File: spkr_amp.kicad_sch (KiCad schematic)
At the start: 6 parts, among them U2 TPA2006D1DRBR

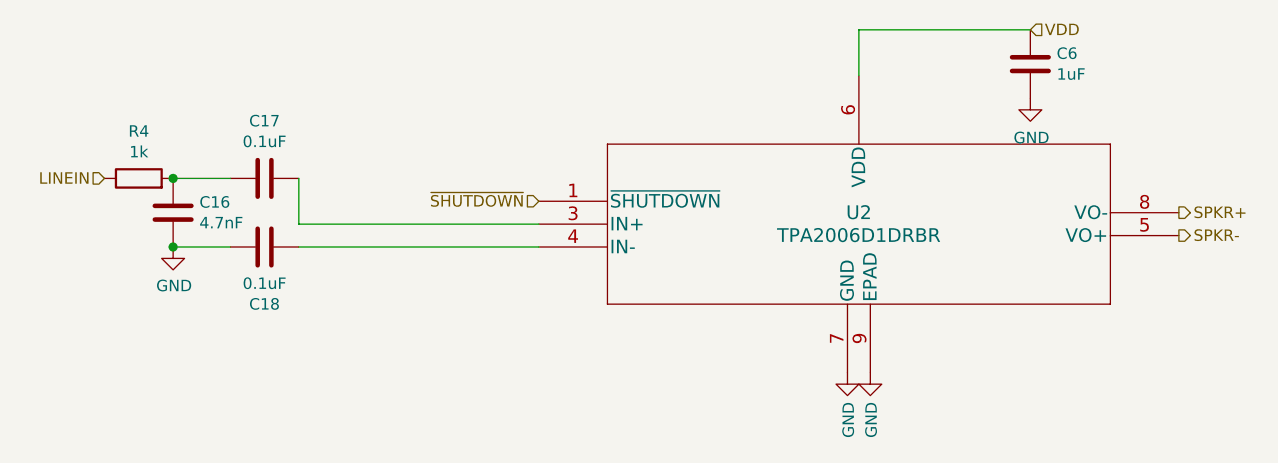
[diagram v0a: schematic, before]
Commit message: Start refactoring board to use Radxa Rock 3 Compute Module instead of Raspberry Pi CM4.
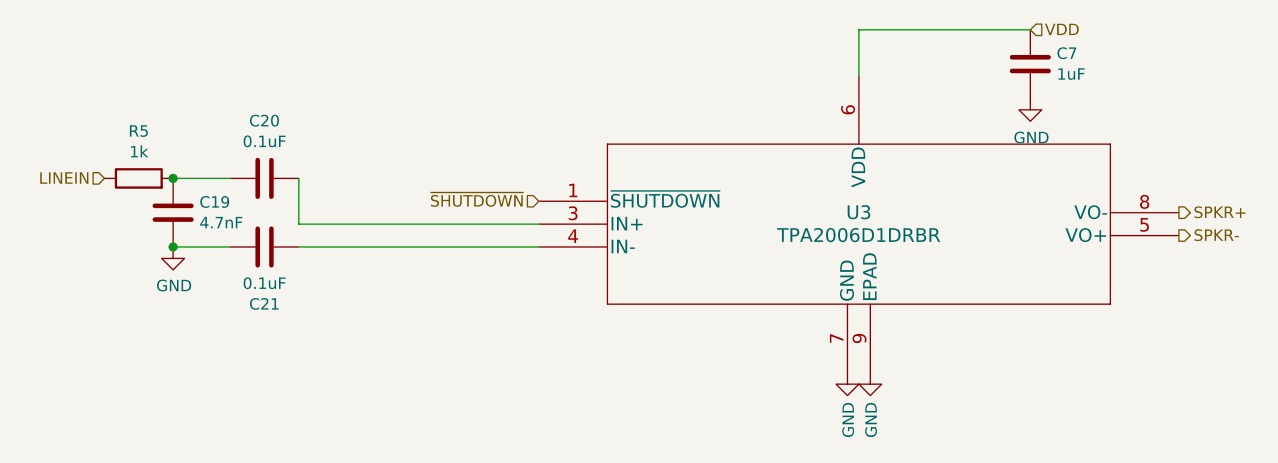
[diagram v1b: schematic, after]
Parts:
- renumbered C16 to C19, C17 to C20, C18 to C21, C6 to C7, R4 to R5, U2 to U3
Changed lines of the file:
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@@
   (symbol (lib_id "Device:R") (at 91.44 78.74 90)
     (in_bom yes) (on_board yes)
-    (property "Reference" "R4" (id 0) (at 91.44 73.5138 90))
+    (property "Reference" "R5" (id 0) (at 91.44 73.5138 90))
     (property "Value" "1k" (id 1) (at 91.44 75.812 90))
     (property "Footprint" "Resistor_SMD:R_0402_1005Metric" (id 2) (at 91.44 80.518 90)
@@
   (symbol (lib_id "Device:C") (at 95.25 82.55 0)
     (in_bom yes) (on_board yes)
-    (property "Reference" "C16" (id 0) (at 98.1711 81.4006 0)
+    (property "Reference" "C19" (id 0) (at 98.1711 81.4006 0)
       (effects (font (size 1.27 1.27)) (justify left))
     )
@@
   (symbol (lib_id "Device:C") (at 105.41 78.74 90)
     (in_bom yes) (on_board yes)
-    (property "Reference" "C17" (id 0) (at 105.41 72.3708 90))
+    (property "Reference" "C20" (id 0) (at 105.41 72.3708 90))
     (property "Value" "0.1uF" (id 1) (at 105.41 74.669 90))
     (property "Footprint" "Capacitor_SMD:C_0402_1005Metric" (id 2) (at 109.22 77.7748 0)
@@
   (symbol (lib_id "Device:C") (at 105.41 86.36 90)
     (in_bom yes) (on_board yes)
-    (property "Reference" "C18" (id 0) (at 105.41 92.7292 90))
+    (property "Reference" "C21" (id 0) (at 105.41 92.7292 90))
     (property "Value" "0.1uF" (id 1) (at 105.41 90.43 90))
     (property "Footprint" "Capacitor_SMD:C_0402_1005Metric" (id 2) (at 109.22 85.3948 0)
@@
   (symbol (lib_id "Device:C") (at 190.5 66.04 0)
     (in_bom yes) (on_board yes)
-    (property "Reference" "C6" (id 0) (at 193.421 64.8716 0)
+    (property "Reference" "C7" (id 0) (at 193.421 64.8716 0)
       (effects (font (size 1.27 1.27)) (justify left))
     )
@@
   (symbol (lib_id "TPA2006D1DRBR:TPA2006D1DRBR") (at 171.45 83.82 0)
     (in_bom yes) (on_board yes)
-    (property "Reference" "U2" (id 0) (at 171.45 82.55 0)
+    (property "Reference" "U3" (id 0) (at 171.45 82.55 0)
       (effects (font (size 1.524 1.524)))
     )

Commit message: WIP: start reworking board to use CM4 instead of 40-pin connector
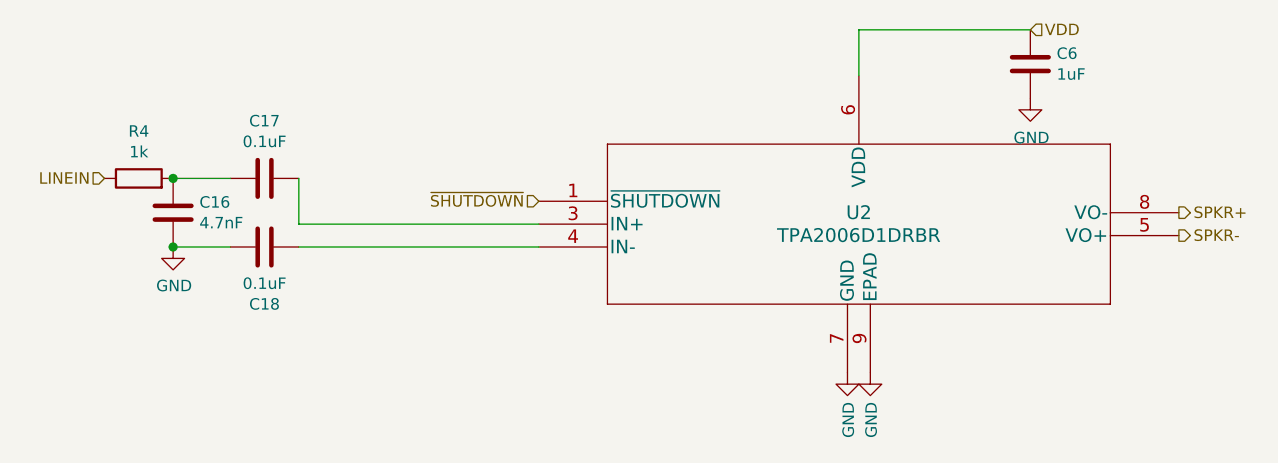
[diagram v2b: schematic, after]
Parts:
- renumbered C19 to C16, C20 to C17, C21 to C18, C7 to C6, R5 to R4, U3 to U2
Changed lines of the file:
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@@
   (symbol (lib_id "Device:R") (at 91.44 78.74 90)
     (in_bom yes) (on_board yes)
-    (property "Reference" "R5" (id 0) (at 91.44 73.5138 90))
+    (property "Reference" "R4" (id 0) (at 91.44 73.5138 90))
     (property "Value" "1k" (id 1) (at 91.44 75.812 90))
     (property "Footprint" "Resistor_SMD:R_0402_1005Metric" (id 2) (at 91.44 80.518 90)
@@
   (symbol (lib_id "Device:C") (at 95.25 82.55 0)
     (in_bom yes) (on_board yes)
-    (property "Reference" "C19" (id 0) (at 98.1711 81.4006 0)
+    (property "Reference" "C16" (id 0) (at 98.1711 81.4006 0)
       (effects (font (size 1.27 1.27)) (justify left))
     )
@@
   (symbol (lib_id "Device:C") (at 105.41 78.74 90)
     (in_bom yes) (on_board yes)
-    (property "Reference" "C20" (id 0) (at 105.41 72.3708 90))
+    (property "Reference" "C17" (id 0) (at 105.41 72.3708 90))
     (property "Value" "0.1uF" (id 1) (at 105.41 74.669 90))
     (property "Footprint" "Capacitor_SMD:C_0402_1005Metric" (id 2) (at 109.22 77.7748 0)
@@
   (symbol (lib_id "Device:C") (at 105.41 86.36 90)
     (in_bom yes) (on_board yes)
-    (property "Reference" "C21" (id 0) (at 105.41 92.7292 90))
+    (property "Reference" "C18" (id 0) (at 105.41 92.7292 90))
     (property "Value" "0.1uF" (id 1) (at 105.41 90.43 90))
     (property "Footprint" "Capacitor_SMD:C_0402_1005Metric" (id 2) (at 109.22 85.3948 0)
@@
   (symbol (lib_id "Device:C") (at 190.5 66.04 0)
     (in_bom yes) (on_board yes)
-    (property "Reference" "C7" (id 0) (at 193.421 64.8716 0)
+    (property "Reference" "C6" (id 0) (at 193.421 64.8716 0)
       (effects (font (size 1.27 1.27)) (justify left))
     )
@@
   (symbol (lib_id "TPA2006D1DRBR:TPA2006D1DRBR") (at 171.45 83.82 0)
     (in_bom yes) (on_board yes)
-    (property "Reference" "U3" (id 0) (at 171.45 82.55 0)
+    (property "Reference" "U2" (id 0) (at 171.45 82.55 0)
       (effects (font (size 1.524 1.524)))
     )

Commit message: WIP: Flip the touchscreen connectors. Fixes #2.
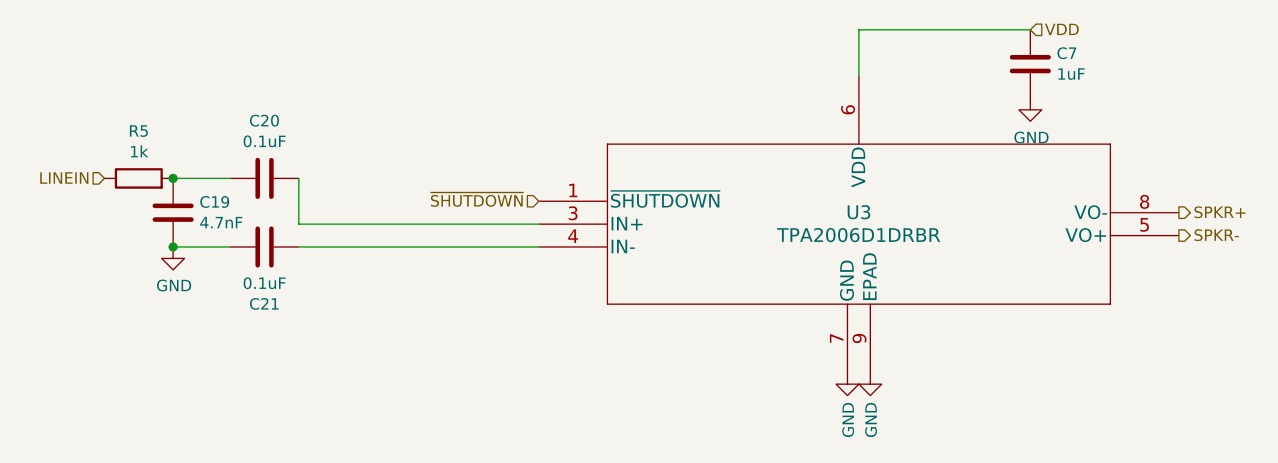
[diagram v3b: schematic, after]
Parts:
- renumbered C16 to C19, C17 to C20, C18 to C21, C6 to C7, R4 to R5, U2 to U3
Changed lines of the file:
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@@
   (symbol (lib_id "power:GND") (at 95.25 86.36 0)
     (in_bom yes) (on_board yes)
-    (property "Reference" "#PWR0112" (id 0) (at 95.25 92.71 0)
+    (property "Reference" "#PWR0105" (id 0) (at 95.25 92.71 0)
       (effects (font (size 1.27 1.27)) hide)
     )
@@
   (symbol (lib_id "power:GND") (at 170.18 100.33 0)
     (in_bom yes) (on_board yes)
-    (property "Reference" "#PWR0116" (id 0) (at 170.18 106.68 0)
+    (property "Reference" "#PWR0107" (id 0) (at 170.18 106.68 0)
       (effects (font (size 1.27 1.27)) hide)
     )
@@
   (symbol (lib_id "power:GND") (at 172.72 100.33 0)
     (in_bom yes) (on_board yes)
-    (property "Reference" "#PWR0117" (id 0) (at 172.72 106.68 0)
+    (property "Reference" "#PWR0108" (id 0) (at 172.72 106.68 0)
       (effects (font (size 1.27 1.27)) hide)
     )
@@
   (symbol (lib_id "power:GND") (at 190.5 69.85 0)
     (in_bom yes) (on_board yes)
-    (property "Reference" "#PWR0118" (id 0) (at 190.5 76.2 0)
+    (property "Reference" "#PWR0110" (id 0) (at 190.5 76.2 0)
       (effects (font (size 1.27 1.27)) hide)
     )
@@
   (symbol (lib_id "Device:R") (at 91.44 78.74 90)
     (in_bom yes) (on_board yes)
-    (property "Reference" "R4" (id 0) (at 91.44 73.5138 90))
+    (property "Reference" "R5" (id 0) (at 91.44 73.5138 90))
     (property "Value" "1k" (id 1) (at 91.44 75.812 90))
     (property "Footprint" "Resistor_SMD:R_0402_1005Metric" (id 2) (at 91.44 80.518 90)
@@
   (symbol (lib_id "Device:C") (at 95.25 82.55 0)
     (in_bom yes) (on_board yes)
-    (property "Reference" "C16" (id 0) (at 98.1711 81.4006 0)
+    (property "Reference" "C19" (id 0) (at 98.1711 81.4006 0)
       (effects (font (size 1.27 1.27)) (justify left))
     )
@@
   (symbol (lib_id "Device:C") (at 105.41 78.74 90)
     (in_bom yes) (on_board yes)
-    (property "Reference" "C17" (id 0) (at 105.41 72.3708 90))
+    (property "Reference" "C20" (id 0) (at 105.41 72.3708 90))
     (property "Value" "0.1uF" (id 1) (at 105.41 74.669 90))
     (property "Footprint" "Capacitor_SMD:C_0402_1005Metric" (id 2) (at 109.22 77.7748 0)
@@
   (symbol (lib_id "Device:C") (at 105.41 86.36 90)
     (in_bom yes) (on_board yes)
-    (property "Reference" "C18" (id 0) (at 105.41 92.7292 90))
+    (property "Reference" "C21" (id 0) (at 105.41 92.7292 90))
     (property "Value" "0.1uF" (id 1) (at 105.41 90.43 90))
     (property "Footprint" "Capacitor_SMD:C_0402_1005Metric" (id 2) (at 109.22 85.3948 0)
@@
   (symbol (lib_id "Device:C") (at 190.5 66.04 0)
     (in_bom yes) (on_board yes)
-    (property "Reference" "C6" (id 0) (at 193.421 64.8716 0)
+    (property "Reference" "C7" (id 0) (at 193.421 64.8716 0)
       (effects (font (size 1.27 1.27)) (justify left))
     )
@@
   (symbol (lib_id "TPA2006D1DRBR:TPA2006D1DRBR") (at 171.45 83.82 0)
     (in_bom yes) (on_board yes)
-    (property "Reference" "U2" (id 0) (at 171.45 82.55 0)
+    (property "Reference" "U3" (id 0) (at 171.45 82.55 0)
       (effects (font (size 1.524 1.524)))
     )

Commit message: Add dock connector, battery pads, and ambient light sensor/compass connector. Switch Pi GPIO header from from THT to SMT so it is easier to place/route. Route differential signals for LVDS converter.
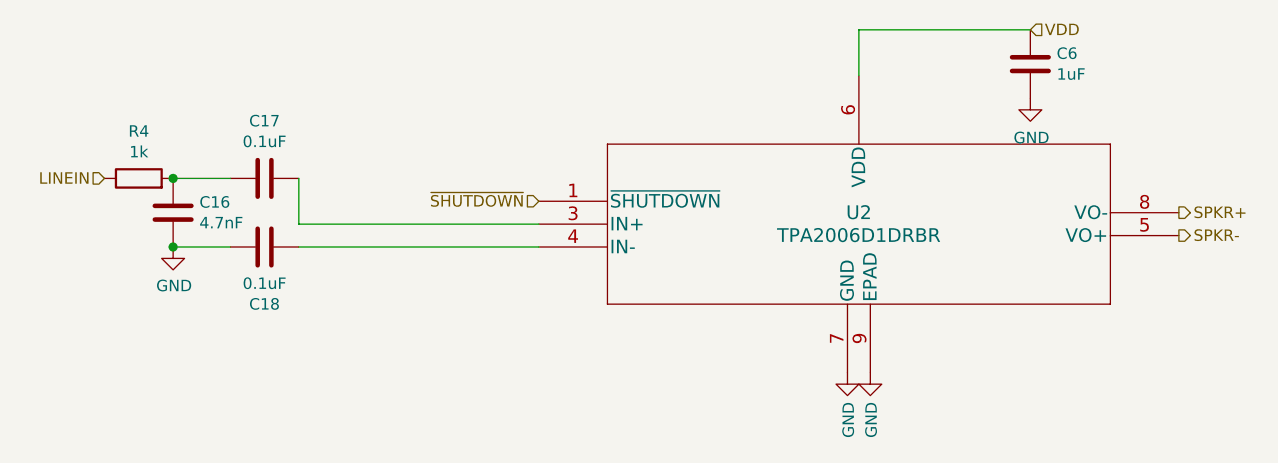
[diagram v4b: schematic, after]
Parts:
- renumbered C19 to C16, C20 to C17, C21 to C18, C7 to C6, R5 to R4, U3 to U2
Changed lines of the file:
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@@
   (symbol (lib_id "power:GND") (at 95.25 86.36 0)
     (in_bom yes) (on_board yes)
-    (property "Reference" "#PWR0105" (id 0) (at 95.25 92.71 0)
+    (property "Reference" "#PWR0112" (id 0) (at 95.25 92.71 0)
       (effects (font (size 1.27 1.27)) hide)
     )
@@
   (symbol (lib_id "power:GND") (at 170.18 100.33 0)
     (in_bom yes) (on_board yes)
-    (property "Reference" "#PWR0107" (id 0) (at 170.18 106.68 0)
+    (property "Reference" "#PWR0116" (id 0) (at 170.18 106.68 0)
       (effects (font (size 1.27 1.27)) hide)
     )
@@
   (symbol (lib_id "power:GND") (at 172.72 100.33 0)
     (in_bom yes) (on_board yes)
-    (property "Reference" "#PWR0108" (id 0) (at 172.72 106.68 0)
+    (property "Reference" "#PWR0117" (id 0) (at 172.72 106.68 0)
       (effects (font (size 1.27 1.27)) hide)
     )
@@
   (symbol (lib_id "power:GND") (at 190.5 69.85 0)
     (in_bom yes) (on_board yes)
-    (property "Reference" "#PWR0110" (id 0) (at 190.5 76.2 0)
+    (property "Reference" "#PWR0118" (id 0) (at 190.5 76.2 0)
       (effects (font (size 1.27 1.27)) hide)
     )
@@
   (symbol (lib_id "Device:R") (at 91.44 78.74 90)
     (in_bom yes) (on_board yes)
-    (property "Reference" "R5" (id 0) (at 91.44 73.5138 90))
+    (property "Reference" "R4" (id 0) (at 91.44 73.5138 90))
     (property "Value" "1k" (id 1) (at 91.44 75.812 90))
     (property "Footprint" "Resistor_SMD:R_0402_1005Metric" (id 2) (at 91.44 80.518 90)
@@
   (symbol (lib_id "Device:C") (at 95.25 82.55 0)
     (in_bom yes) (on_board yes)
-    (property "Reference" "C19" (id 0) (at 98.1711 81.4006 0)
+    (property "Reference" "C16" (id 0) (at 98.1711 81.4006 0)
       (effects (font (size 1.27 1.27)) (justify left))
     )
@@
   (symbol (lib_id "Device:C") (at 105.41 78.74 90)
     (in_bom yes) (on_board yes)
-    (property "Reference" "C20" (id 0) (at 105.41 72.3708 90))
+    (property "Reference" "C17" (id 0) (at 105.41 72.3708 90))
     (property "Value" "0.1uF" (id 1) (at 105.41 74.669 90))
     (property "Footprint" "Capacitor_SMD:C_0402_1005Metric" (id 2) (at 109.22 77.7748 0)
@@
   (symbol (lib_id "Device:C") (at 105.41 86.36 90)
     (in_bom yes) (on_board yes)
-    (property "Reference" "C21" (id 0) (at 105.41 92.7292 90))
+    (property "Reference" "C18" (id 0) (at 105.41 92.7292 90))
     (property "Value" "0.1uF" (id 1) (at 105.41 90.43 90))
     (property "Footprint" "Capacitor_SMD:C_0402_1005Metric" (id 2) (at 109.22 85.3948 0)
@@
   (symbol (lib_id "Device:C") (at 190.5 66.04 0)
     (in_bom yes) (on_board yes)
-    (property "Reference" "C7" (id 0) (at 193.421 64.8716 0)
+    (property "Reference" "C6" (id 0) (at 193.421 64.8716 0)
       (effects (font (size 1.27 1.27)) (justify left))
     )
@@
   (symbol (lib_id "TPA2006D1DRBR:TPA2006D1DRBR") (at 171.45 83.82 0)
     (in_bom yes) (on_board yes)
-    (property "Reference" "U3" (id 0) (at 171.45 82.55 0)
+    (property "Reference" "U2" (id 0) (at 171.45 82.55 0)
       (effects (font (size 1.524 1.524)))
     )
